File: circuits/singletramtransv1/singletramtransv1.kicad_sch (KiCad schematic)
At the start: 21 parts, among them J1 Power 9V, J2 Signal in, Q1 S9013

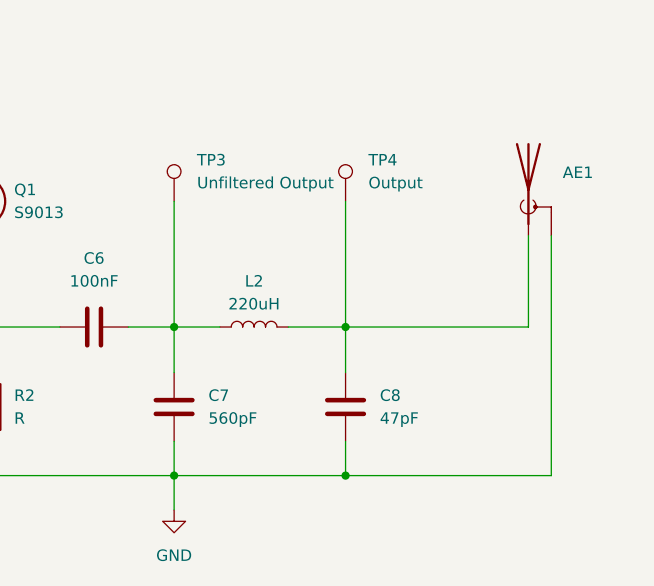
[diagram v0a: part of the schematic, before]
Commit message: Updating the single transistor AM test transmitter project
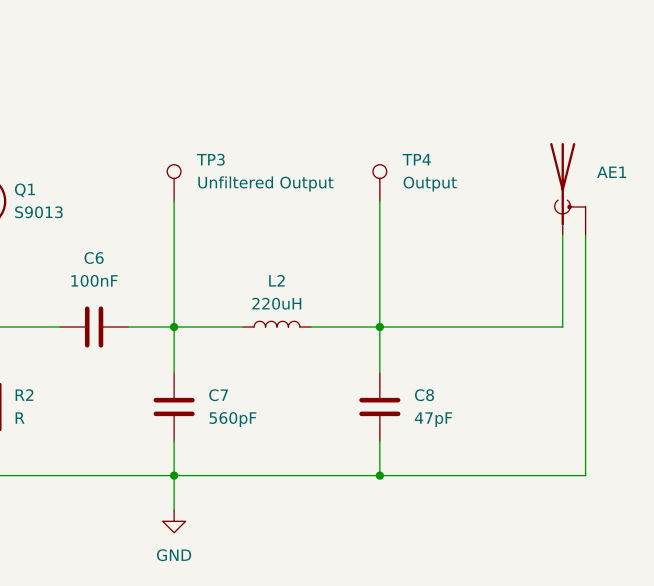
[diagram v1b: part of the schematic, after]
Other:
- moved on the sheet: AE1, C8, L2, TP4
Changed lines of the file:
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@@
 	)
 	(junction
-		(at 212.09 96.52)
+		(at 215.9 96.52)
 		(diameter 0)
 		(color 0 0 0 0)
 	)
 	(junction
-		(at 212.09 113.03)
+		(at 215.9 113.03)
 		(diameter 0)
 		(color 0 0 0 0)
@@
 	(wire
 		(pts
-			(xy 193.04 96.52) (xy 198.12 96.52)
+			(xy 193.04 96.52) (xy 200.66 96.52)
 		)
 		(stroke
@@
 	(wire
 		(pts
-			(xy 212.09 109.22) (xy 212.09 113.03)
+			(xy 215.9 109.22) (xy 215.9 113.03)
 		)
 		(stroke
@@
 	(wire
 		(pts
-			(xy 205.74 96.52) (xy 212.09 96.52)
-		)
-		(stroke
-			(width 0)
-			(type default)
-		)
-	)
-	(wire
-		(pts
-			(xy 212.09 82.55) (xy 212.09 96.52)
+			(xy 215.9 82.55) (xy 215.9 96.52)
 		)
 		(stroke
@@
 	(wire
 		(pts
-			(xy 232.41 96.52) (xy 212.09 96.52)
+			(xy 236.22 96.52) (xy 215.9 96.52)
 		)
 		(stroke
@@
 	(wire
 		(pts
-			(xy 234.95 86.36) (xy 234.95 113.03)
+			(xy 208.28 96.52) (xy 215.9 96.52)
+		)
+		(stroke
+			(width 0)
+			(type default)
+		)
+	)
+	(wire
+		(pts
+			(xy 238.76 86.36) (xy 238.76 113.03)
 		)
 		(stroke
@@
 	(wire
 		(pts
-			(xy 232.41 86.36) (xy 232.41 96.52)
+			(xy 236.22 86.36) (xy 236.22 96.52)
 		)
 		(stroke
@@
 	(wire
 		(pts
+			(xy 193.04 113.03) (xy 215.9 113.03)
+		)
+		(stroke
+			(width 0)
+			(type default)
+		)
+	)
+	(wire
+		(pts
 			(xy 80.01 107.95) (xy 97.79 107.95)
 		)
@@
 	(wire
 		(pts
-			(xy 212.09 96.52) (xy 212.09 101.6)
+			(xy 215.9 96.52) (xy 215.9 101.6)
 		)
 		(stroke
@@
 	(wire
 		(pts
-			(xy 212.09 113.03) (xy 193.04 113.03)
-		)
-		(stroke
-			(width 0)
-			(type default)
-		)
-	)
-	(wire
-		(pts
 			(xy 144.78 107.95) (xy 144.78 96.52)
 		)
@@
 	(wire
 		(pts
-			(xy 234.95 113.03) (xy 212.09 113.03)
+			(xy 238.76 113.03) (xy 215.9 113.03)
 		)
 		(stroke
@@
 	(symbol
 		(lib_id "Connector:TestPoint")
-		(at 212.09 82.55 0)
+		(at 215.9 82.55 0)
 		(unit 1)
 		(exclude_from_sim no)
@@
 		(fields_autoplaced yes)
 		(property "Reference" "TP4"
-			(at 214.63 77.9779 0)
+			(at 218.44 77.9779 0)
 			(effects
 				(font
@@
 		)
 		(property "Value" "Output"
-			(at 214.63 80.5179 0)
+			(at 218.44 80.5179 0)
 			(effects
 				(font
@@
 		)
 		(property "Footprint" "TestPoint:TestPoint_Loop_D2.50mm_Drill1.0mm"
-			(at 217.17 82.55 0)
+			(at 220.98 82.55 0)
 			(effects
 				(font
@@
 		)
 		(property "Datasheet" "~"
-			(at 217.17 82.55 0)
+			(at 220.98 82.55 0)
 			(effects
 				(font
@@
 		)
 		(property "Description" "test point"
-			(at 212.09 82.55 0)
+			(at 215.9 82.55 0)
 			(effects
 				(font
@@
 	(symbol
 		(lib_id "Device:L")
-		(at 201.93 96.52 90)
+		(at 204.47 96.52 90)
 		(unit 1)
 		(exclude_from_sim no)
@@
 		(fields_autoplaced yes)
 		(property "Reference" "L2"
-			(at 201.93 91.44 90)
+			(at 204.47 91.44 90)
 			(effects
 				(font
@@
 		)
 		(property "Value" "220uH"
-			(at 201.93 93.98 90)
+			(at 204.47 93.98 90)
 			(effects
 				(font
@@
 		)
 		(property "Footprint" "Inductor_THT:L_Axial_L11.0mm_D4.5mm_P15.24mm_Horizontal_Fastron_MECC"
-			(at 201.93 96.52 0)
+			(at 204.47 96.52 0)
 			(effects
 				(font
@@
 		)
 		(property "Datasheet" "~"
-			(at 201.93 96.52 0)
+			(at 204.47 96.52 0)
 			(effects
 				(font
@@
 		)
 		(property "Description" "Inductor"
-			(at 201.93 96.52 0)
+			(at 204.47 96.52 0)
 			(effects
 				(font
@@
 	(symbol
 		(lib_id "Device:C")
-		(at 212.09 105.41 0)
-		(unit 1)
-		(exclude_from_sim no)
-		(in_bom yes)
-		(on_board yes)
-		(dnp no)
-		(fields_autoplaced yes)
+		(at 215.9 105.41 0)
+		(unit 1)
+		(exclude_from_sim no)
+		(in_bom yes)
+		(on_board yes)
+		(dnp no)
 		(property "Reference" "C8"
-			(at 215.9 104.1399 0)
+			(at 219.71 104.1399 0)
 			(effects
 				(font
@@
 		)
 		(property "Value" "47pF"
-			(at 215.9 106.6799 0)
+			(at 219.71 106.6799 0)
 			(effects
 				(font
@@
 		)
 		(property "Footprint" "Capacitor_SMD:C_0805_2012Metric_Pad1.18x1.45mm_HandSolder"
-			(at 213.0552 109.22 0)
+			(at 216.8652 109.22 0)
 			(effects
 				(font
@@
 		)
 		(property "Datasheet" "~"
-			(at 212.09 105.41 0)
+			(at 215.9 105.41 0)
 			(effects
 				(font
@@
 		)
 		(property "Description" "Unpolarized capacitor"
-			(at 212.09 105.41 0)
+			(at 215.9 105.41 0)
 			(effects
 				(font
@@
 	(symbol
 		(lib_id "Device:Antenna_Shield")
-		(at 232.41 81.28 0)
+		(at 236.22 81.28 0)
 		(unit 1)
 		(exclude_from_sim no)
@@
 		(fields_autoplaced yes)
 		(property "Reference" "AE1"
-			(at 236.22 79.3749 0)
+			(at 240.03 79.3749 0)
 			(effects
 				(font
@@
 		)
 		(property "Value" "~"
-			(at 236.22 81.9149 0)
+			(at 240.03 81.9149 0)
 			(effects
 				(font
@@
 		)
 		(property "Footprint" "gos:COAX4GND_132203RP_AMP"
-			(at 232.41 78.74 0)
+			(at 236.22 78.74 0)
 			(effects
 				(font
@@
 		)
 		(property "Datasheet" "~"
-			(at 232.41 78.74 0)
+			(at 236.22 78.74 0)
 			(effects
 				(font
@@
 		)
 		(property "Description" "Antenna with extra pin for shielding"
-			(at 232.41 81.28 0)
-			(effects
-				(font
+			(at 236.22 81.28 0)
+			(effects
+				(font

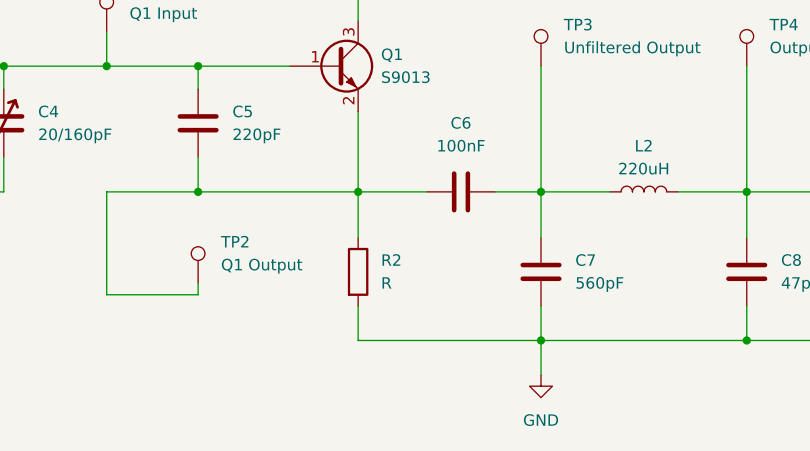
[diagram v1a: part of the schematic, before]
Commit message: Updating the single transistor AM transmitter and adding document for tube amps
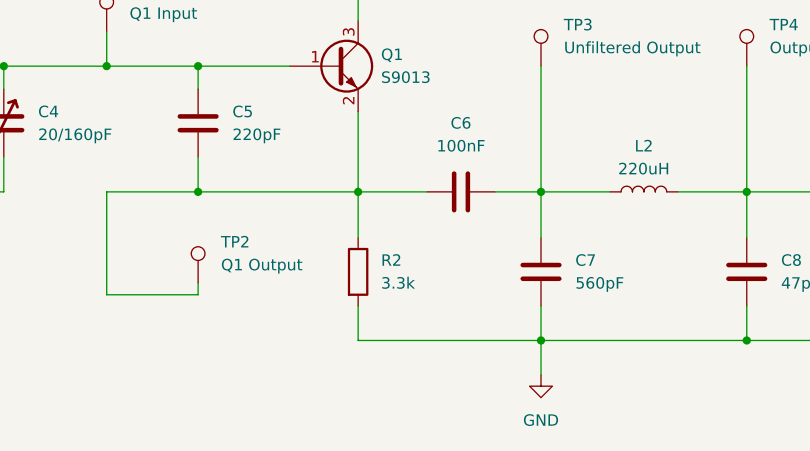
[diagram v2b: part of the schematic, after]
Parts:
- R2: value R -> 3.3k
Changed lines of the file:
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@@
 			)
 		)
-		(property "Value" "R"
+		(property "Value" "3.3k"
 			(at 175.26 106.6799 0)
 			(effects
